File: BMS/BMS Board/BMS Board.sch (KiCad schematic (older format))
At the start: 5 parts

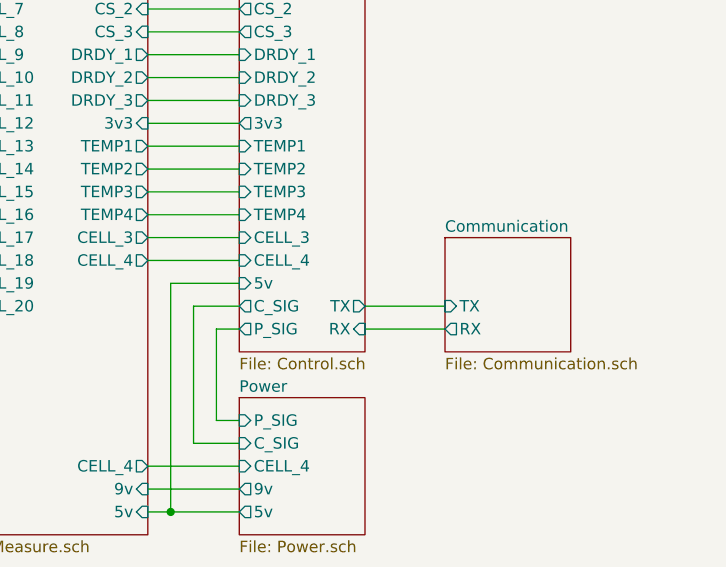
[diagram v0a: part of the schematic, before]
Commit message: changed ui components to be classes instead of methods in Screen class
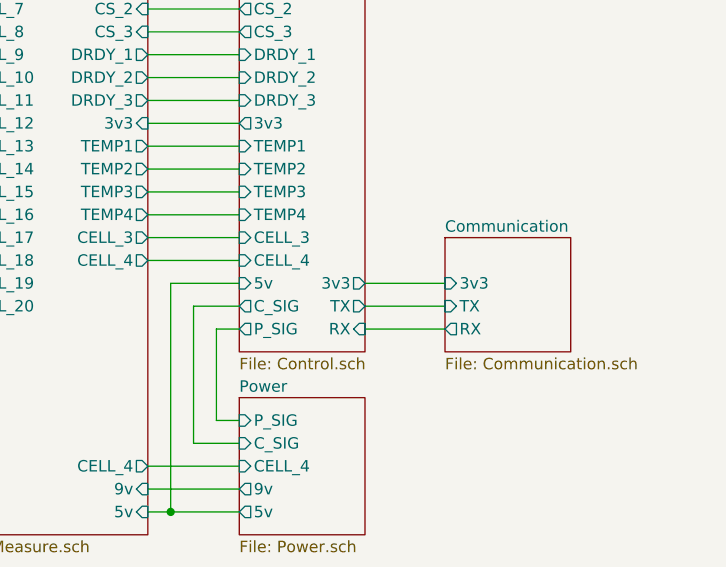
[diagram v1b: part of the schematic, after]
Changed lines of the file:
@@
 F2 "TX" I L 5500 7450 50
 F3 "RX" O L 5500 7550 50
+F4 "3v3" I L 5500 7350 50
 $EndSheet
 $Sheet
@@
 F43 "TEMP4" I L 4600 7050 50
 F44 "CELL_4" I L 4600 7250 50
+F45 "3v3" O R 5150 7350 50
 $EndSheet
 Wire Wire Line
@@
 Wire Wire Line
 	4400 8050 4600 8050
+Wire Wire Line
+	5150 7350 5500 7350
 $EndSCHEMATC

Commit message: workin on BMS also reset my computer so KiCad added some recovery files
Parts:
- PORT1: symbol Molex:430452221 -> BMS-Board-rescue:430452221-Molex
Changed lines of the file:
@@
 	4200 6650 4600 6650
 $Comp
-L Molex:430452221 PORT1
+L BMS-Board-rescue:430452221-Molex PORT1
 U 1 1 5EB58D75
 P 1550 5350
